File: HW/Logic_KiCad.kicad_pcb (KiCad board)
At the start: 2 copper layers, 244 parts, among them J1 USB_B_Micro, Q1 Q_NPN_BCE, Q2 Q_NPN_BCE, Q3 Q_PMOS_DGS, Q4 Q_PMOS_DGS, Q5 Q_PMOS_DGS, Q6 Q_PMOS_DGS, Q7 Q_PMOS_DGS, SW1 SW_SPDT, SW2 button, SW3 button, SW4 button, SW5 button, SW6 button, SW7 button, SW8 button, U1 ESP32-PICO-D4, U2 CP2102N-A01-GQFN28, U3 SY8105, U4 Dual_battery, U5 TP4056

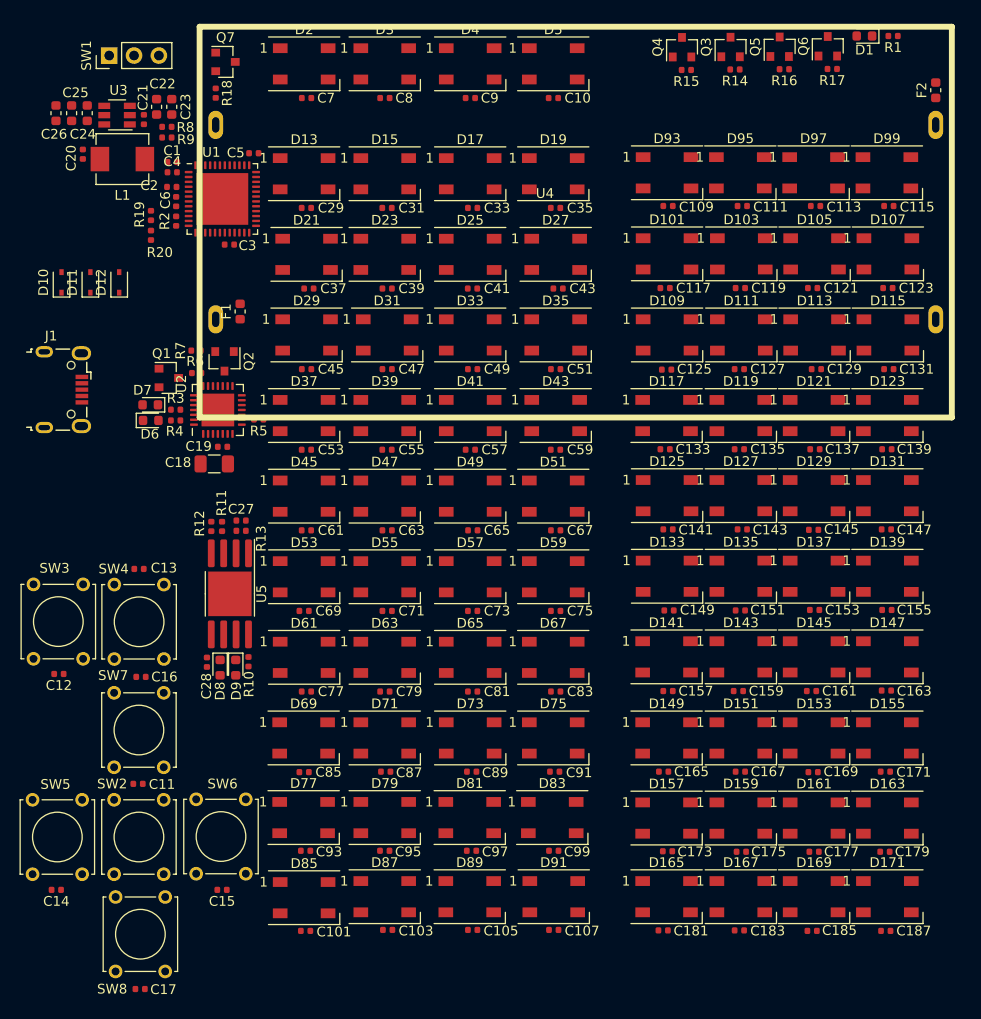
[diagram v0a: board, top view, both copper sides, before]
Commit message: new position of some components
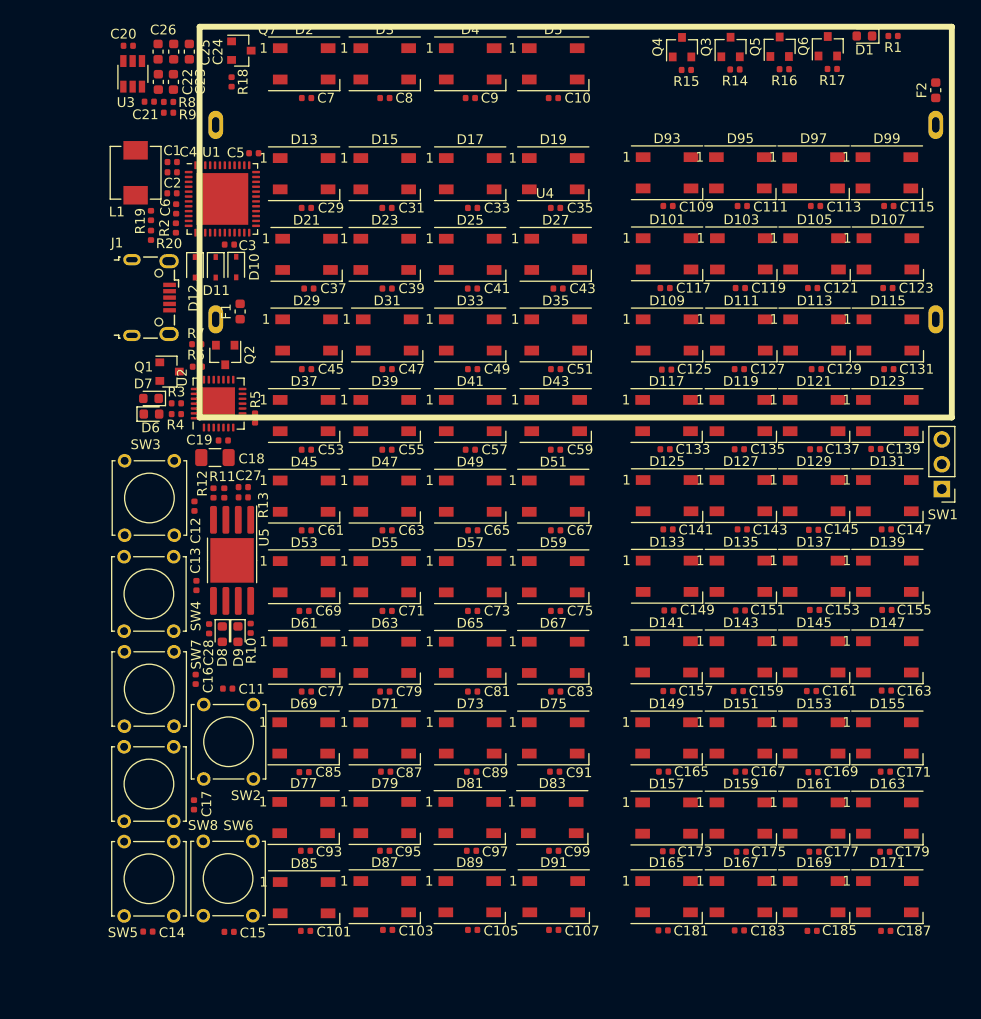
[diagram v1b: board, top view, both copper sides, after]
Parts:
- moved SW1 96.1 mm to (220.0, 83.8), turned to 180 degrees
- moved C12 22.1 mm to (143.5, 85.5), turned to 90 degrees
- moved C17 19.6 mm to (143.5, 116.1), turned to 90 degrees
- moved D10 17.9 mm to (147.8, 61.0), turned to 270 degrees
- moved SW3 15.7 mm to (136.4, 88.5)
- moved SW8 15.4 mm to (136.3, 117.8)
- moved C11 13.4 mm to (146.9, 104.2)
- moved SW2 13.4 mm to (144.5, 113.5)
- moved J1 13.0 mm to (139.1, 64.2)
- moved D11 12.9 mm to (145.7, 61.1), turned to 270 degrees
- moved C25 12.2 mm to (141.4, 39.0)
- moved C26 12.2 mm to (139.8, 39.0)
- moved C24 12.2 mm to (143.0, 39.0)
- moved C20 12.0 mm to (136.8, 38.4), turned to 180 degrees
- moved C14 10.3 mm to (138.8, 129.1)
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
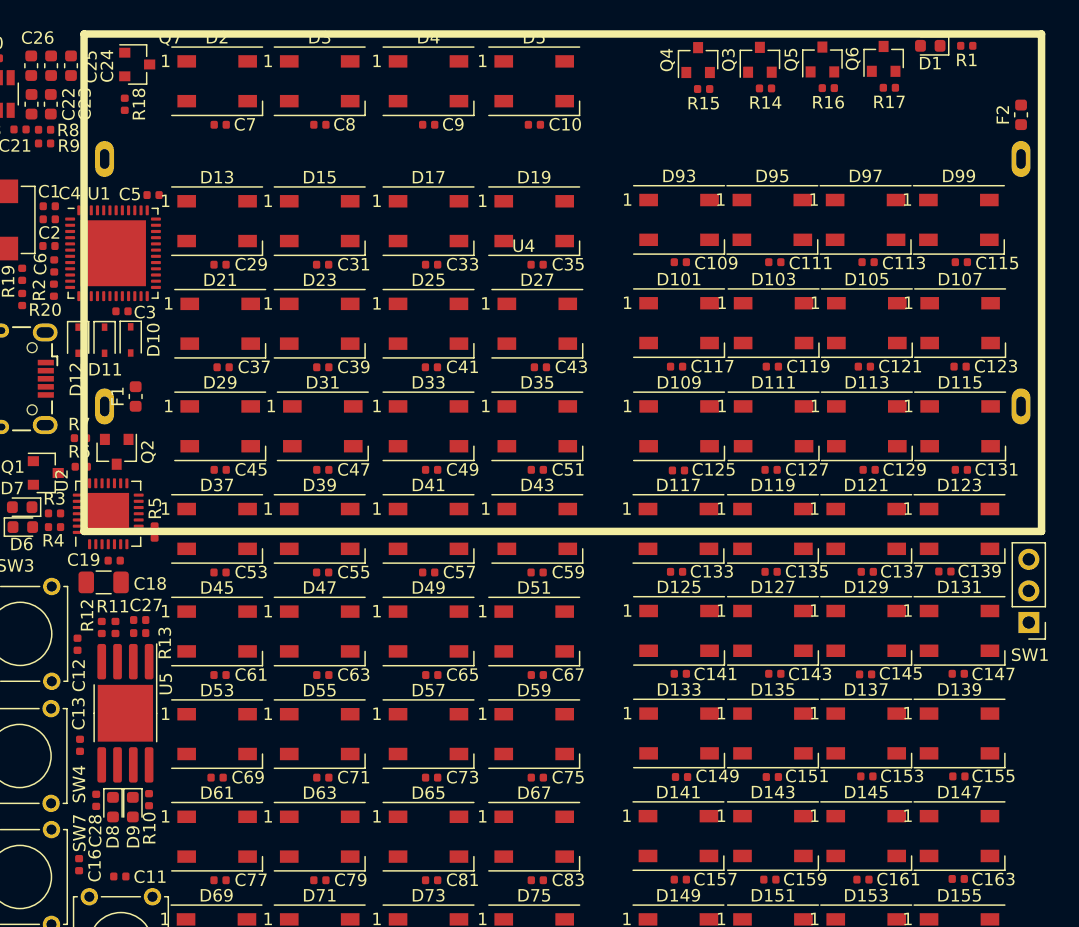
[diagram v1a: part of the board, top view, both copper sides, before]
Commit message: repair package of TP4056
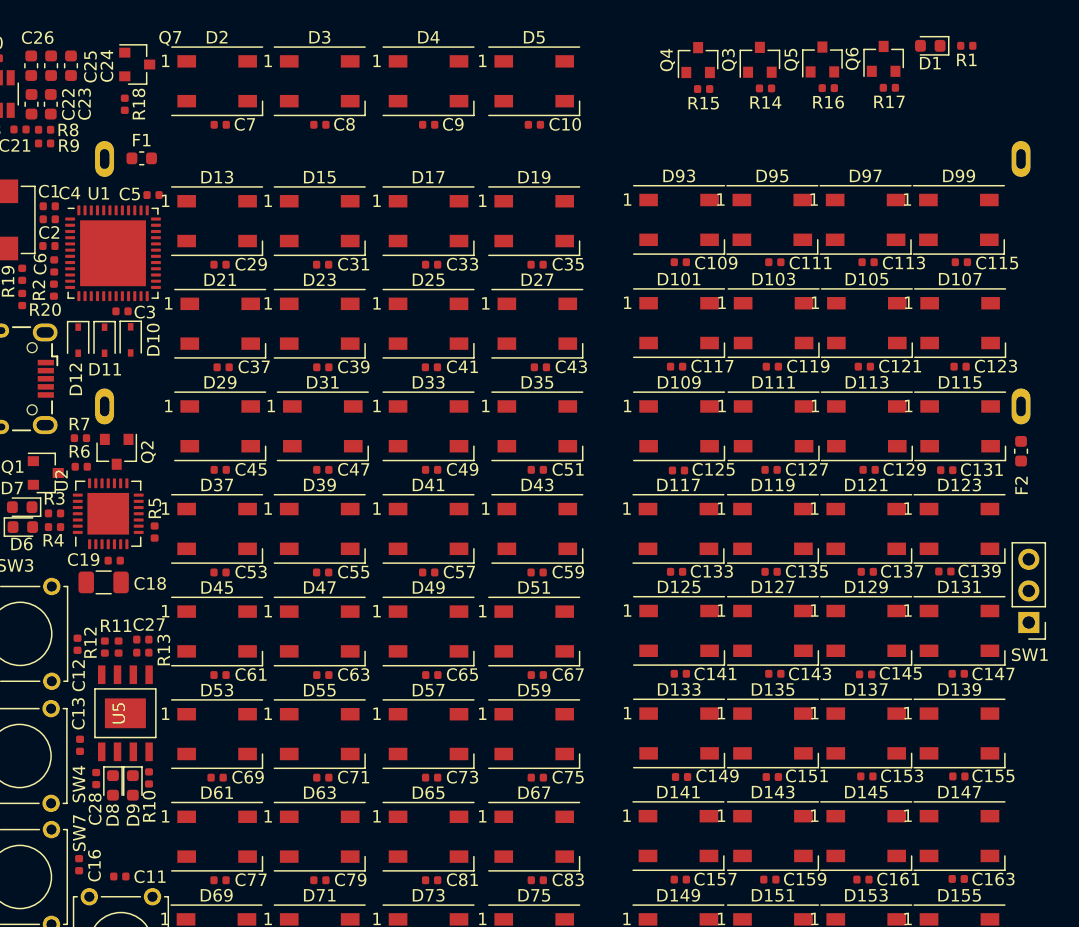
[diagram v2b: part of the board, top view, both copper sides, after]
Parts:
- U4: moved to B.Cu
- U5: footprint Package_SO:SOP-8-1EP_4.57x4.57mm_P1.27mm_EP4.57x4.45mm -> my_library:TP4056
- moved F2 27.0 mm to (219.4, 70.0), turned to 270 degrees
- moved F1 19.2 mm to (148.7, 46.5), turned to 0 degrees
- moved C28 1.75 mm to (145.0, 96.3)
- moved D8 1.75 mm to (146.4, 96.9)
- moved D9 1.75 mm to (148.0, 96.9)
- moved R10 1.75 mm to (149.3, 96.3)
- moved C27 1.59 mm to (148.8, 85.2)
- moved R11 1.59 mm to (146.8, 85.8)
- moved R12 1.59 mm to (145.7, 85.8)
- moved R13 1.59 mm to (148.8, 86.2)
- moved C131 1.18 mm to (213.4, 71.5)
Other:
- copper layers 2 -> 4
- rule trace_min: 0.2 -> 0.09

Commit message: start routing
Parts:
- moved D10 2.10 mm to (145.7, 61.1)
- moved D11 2.05 mm to (147.8, 61.1)
- moved R20 0.13 mm to (139.2, 57.8)
- moved R19 0.13 mm to (139.2, 55.8)
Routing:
- net V_BAT_1: track 0.00 -> 472.8 mm
- net V_BAT_2: track 0.00 -> 386.5 mm
- net V_BAT_3: track 0.00 -> 253.9 mm
- net V_BAT_4: track 0.00 -> 252.7 mm
- net GND: track 0.00 -> 190.4 mm
- net V_BAT: track 0.00 -> 120.7 mm
- net V_BAT_PRIME: track 0.00 -> 120.7 mm
- net D+: track 0.00 -> 8.24 mm
- net VBUS: track 0.00 -> 7.64 mm
- net D-: track 0.00 -> 5.76 mm
- net Net-(F2-Pad1): track 0.00 -> 2.69 mm
- net Net-(F1-Pad1): track 0.00 -> 2.22 mm

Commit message: repair mistake with buttons
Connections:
- C1 pad 2: BTN_END -> +3V3
- C11 pad 2: BTN_END -> BTN_ENTER
- C13 pad 2: BTN_END -> BTN_NEW_GAME
- C14 pad 2: BTN_END -> BTN_SIPKA_VLEVO
- C15 pad 2: BTN_END -> BTN_SIPKA_VPRAVO
- C16 pad 2: BTN_END -> BTN_SIPKA_NAHORU
- C17 pad 2: BTN_END -> BTN_SIPKA_DOLU
- C18 pad 2: BTN_END -> +3V3
- C19 pad 2: BTN_END -> +3V3
- C2 pad 1: BTN_END -> +3V3
- C21 pad 2: BTN_END -> +3V3
- C22 pad 2: BTN_END -> +3V3
- C23 pad 2: BTN_END -> +3V3
- C3 pad 2: BTN_END -> +3V3
- C4 pad 1: BTN_END -> +3V3
- C5 pad 2: BTN_END -> +3V3
- L1 pad 2: BTN_END -> +3V3
- R2 pad 1: BTN_END -> +3V3
- R5 pad 1: BTN_END -> +3V3
- R8 pad 1: BTN_END -> +3V3
- SW2 pad 1: BTN_END -> BTN_ENTER
- SW4 pad 1: BTN_END -> BTN_NEW_GAME
- SW5 pad 1: BTN_END -> BTN_SIPKA_VLEVO
- SW6 pad 1: BTN_END -> BTN_SIPKA_VPRAVO
- SW7 pad 1: BTN_END -> BTN_SIPKA_NAHORU
- SW8 pad 1: BTN_END -> BTN_SIPKA_DOLU
- U1 pad 1: BTN_END -> +3V3
- U1 pad 10: BTN_END -> BTN_SIPKA_DOLU
- U1 pad 12: BTN_END -> BTN_SIPKA_VLEVO
- U1 pad 13: BTN_END -> BTN_SIPKA_VPRAVO
- U1 pad 14: BTN_END -> BTN_ENTER
- U1 pad 16: BTN_END -> BTN_NEW_GAME
- U1 pad 17: BTN_END -> BTN_SIPKA_NAHORU
- U1 pad 19: BTN_END -> +3V3
- U1 pad 3: BTN_END -> +3V3
- U1 pad 37: BTN_END -> +3V3
- U1 pad 4: BTN_END -> +3V3
- U1 pad 43: BTN_END -> +3V3
- U1 pad 46: BTN_END -> +3V3
- U2 pad 6: BTN_END -> +3V3
- U2 pad 7: BTN_END -> +3V3

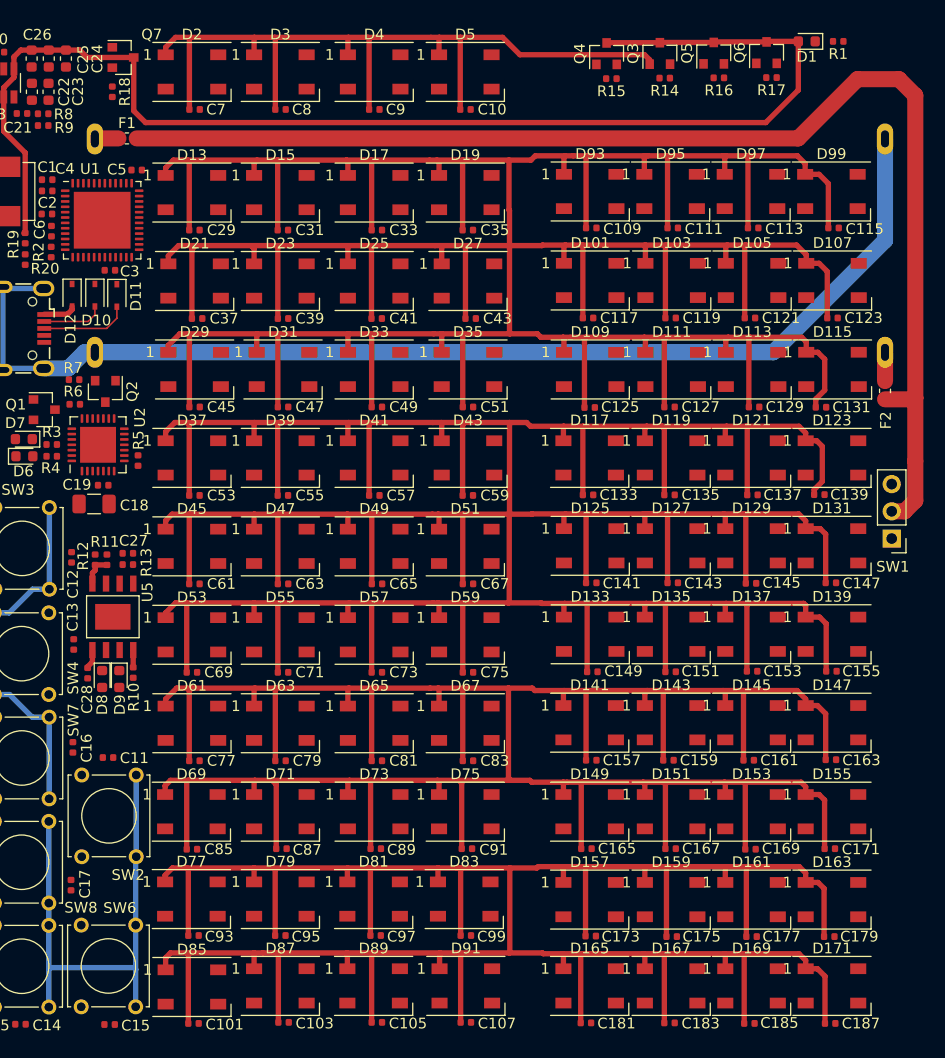
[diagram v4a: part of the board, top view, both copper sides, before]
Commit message: rotate LEDs and capacitors
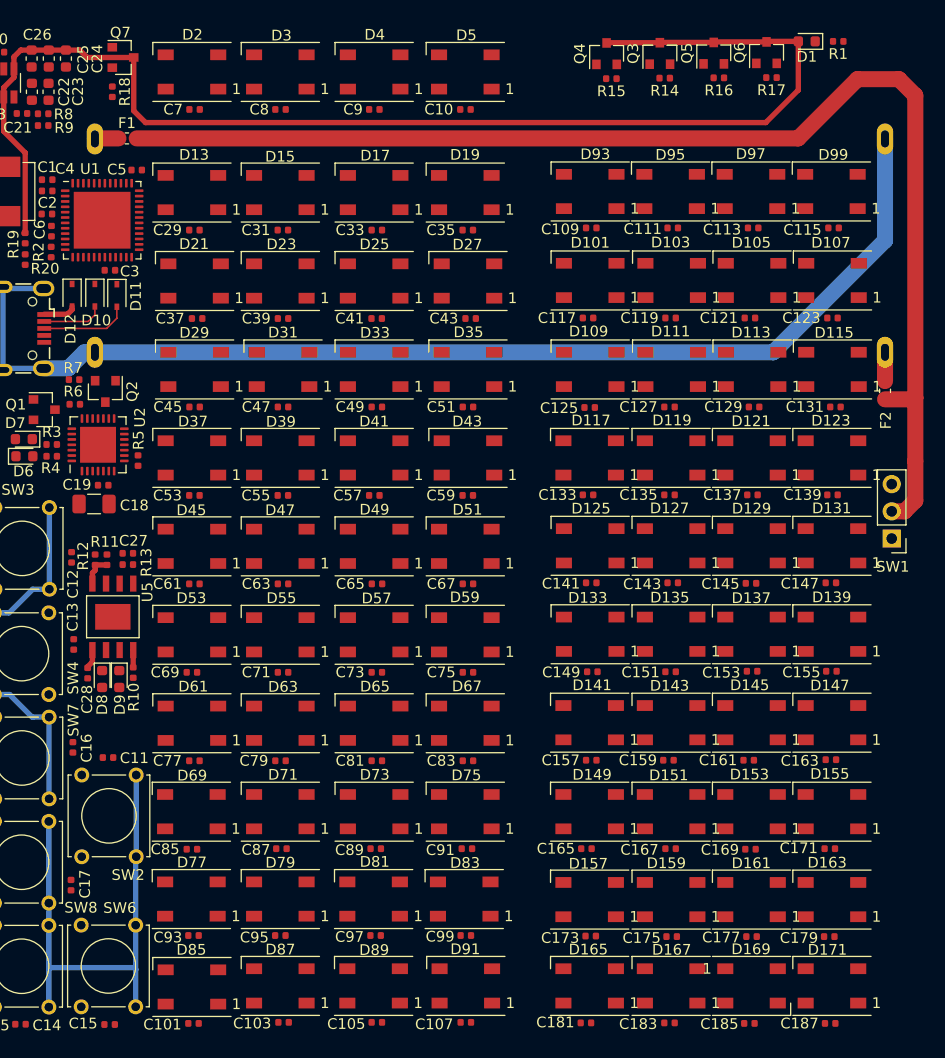
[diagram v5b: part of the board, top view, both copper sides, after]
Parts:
- moved C131 1.35 mm to (214.8, 71.5), turned to 180 degrees
- moved C139 1.23 mm to (214.5, 79.7), turned to 180 degrees
- turned C10 to 180 degrees
- turned C101 to 180 degrees
- turned C103 to 180 degrees
- turned C105 to 180 degrees
- turned C107 to 180 degrees
- turned C109 to 180 degrees
- turned C111 to 180 degrees
- turned C113 to 180 degrees
- turned C115 to 180 degrees
- turned C117 to 180 degrees
- turned C119 to 180 degrees
- turned C121 to 180 degrees
- turned C123 to 180 degrees
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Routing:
- net V_BAT_1: track 472.8 -> 0.00 mm
- net V_BAT_2: track 386.5 -> 0.00 mm
- net V_BAT_3: track 253.9 -> 0.00 mm
- net V_BAT_4: track 252.7 -> 0.00 mm
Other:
- copper layers 4 -> 2
